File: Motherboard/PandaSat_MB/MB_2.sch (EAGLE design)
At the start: 122 parts, among them J1 503182-1852, J10 1445055-5, J2 10118194-0001LF, J3 DCJ0303, J4 1445055-5, J5 1445055-5, J6 1445055-5, J7 BK-18650, J8 1445055-5, J9 1445055-5, Q10 IRLML5103, Q11 IRLML5103, Q13 IRLML2803, Q14 IRLML2803, Q15 IRLML2803, Q16 IRLML5103, Q17 2N5088, Q2 32.768, U1 MAX706R, U11 DRV8848, U12 DRV8848, U13 DRV8848, U2 LTC4121-4.2, U3 LSM9DS1, U4 PE014006, U5 MAX4372TEUK+T, U6 RFM23BP, U7 TPS54226PWPRPWP14_2P31X2P46-L, U8 ATSAMD51, U9 OKL-T3-W12, X1 BU-SMA-V

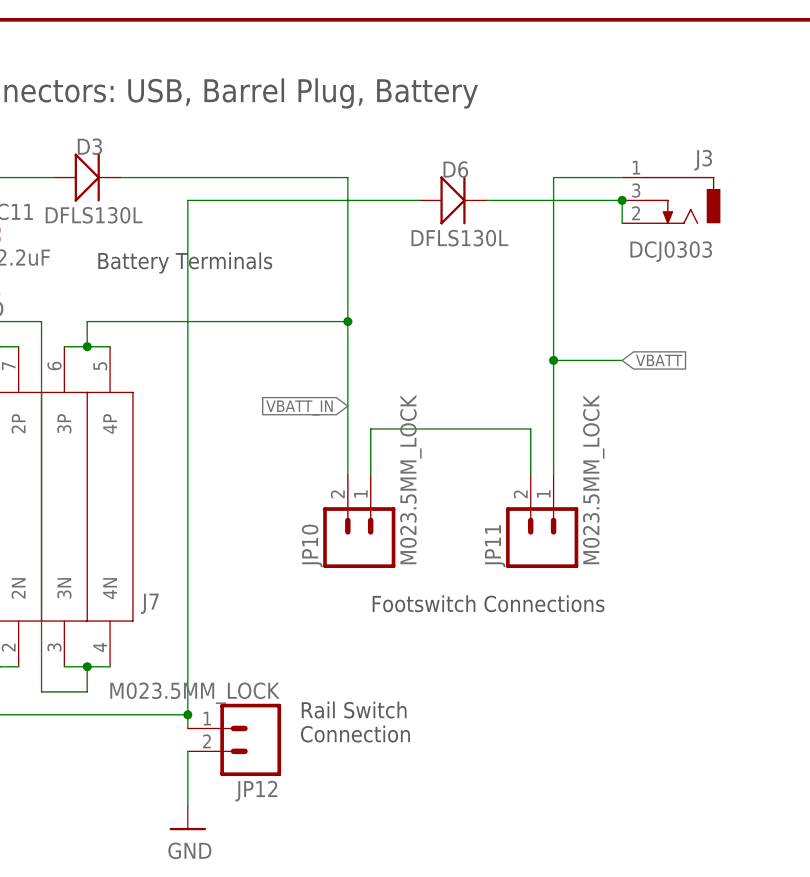
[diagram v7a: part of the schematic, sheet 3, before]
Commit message: Changed diode on power jack
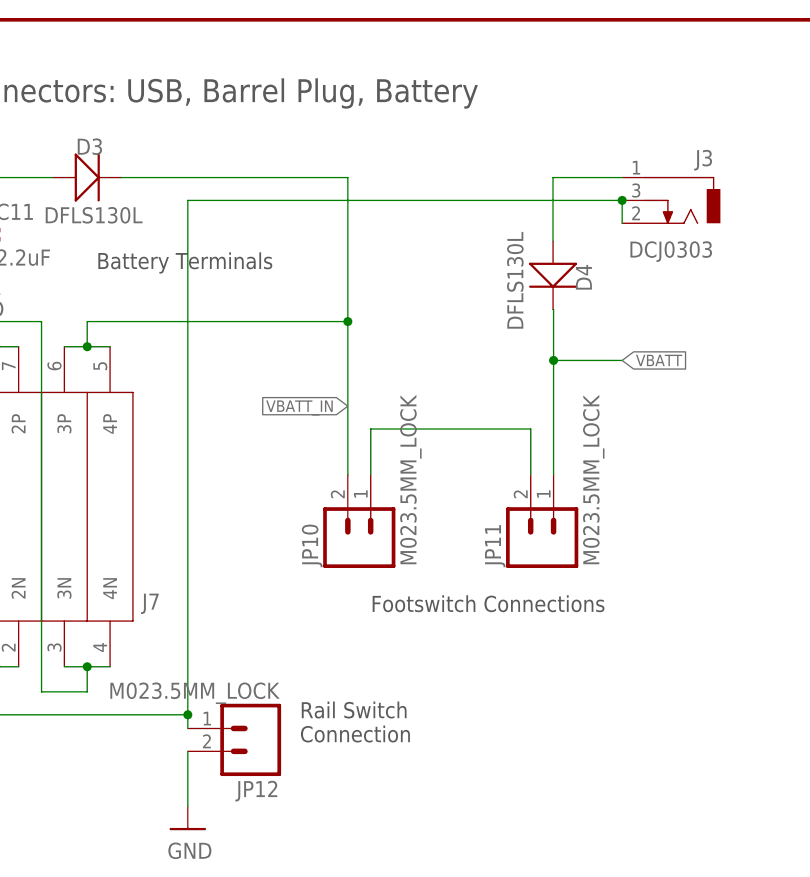
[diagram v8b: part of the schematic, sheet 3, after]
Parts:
- removed D6: DFLS130L, BrownSpaceEngineering:DFLS130L
- added D4: DFLS130L, BrownSpaceEngineering:DFLS130L
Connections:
- net N$30: now also J7.1N, J7.2N, JP12.1; no longer D6.C
- net N$40: now also D4.A, J3.1; no longer D6.A, J7.1N, J7.2N, JP12.1
- net VBATT: now also D4.C; no longer J3.1
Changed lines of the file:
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@@
 <setting verticaltext="up"/>
 </settings>
-<grid distance="2" unitdist="mm" unit="mm" style="lines" multiple="1" display="yes" altdistance="0.01" altunitdist="inch" altunit="inch"/>
+<grid distance="0.01" unitdist="inch" unit="inch" style="lines" multiple="1" display="yes" altdistance="0.01" altunitdist="inch" altunit="inch"/>
 <layers>
 <layer number="1" name="Top" color="35" fill="1" visible="no" active="no"/>
@@
 <part name="D3" library="BrownSpaceEngineering" deviceset="DFLS130L" device="" value="DFLS130L"/>
 <part name="J7" library="pandasat" deviceset="BK-18650" device=""/>
-<part name="D6" library="BrownSpaceEngineering" deviceset="DFLS130L" device="" value="DFLS130L"/>
 <part name="SUPPLY7" library="SparkFun-Aesthetics" deviceset="5V" device=""/>
 <part name="GND32" library="SparkFun-Aesthetics" deviceset="GND" device=""/>
@@
 <part name="GND39" library="supply1" library_urn="urn:adsk.eagle:library:371" deviceset="GND" device=""/>
 <part name="GND40" library="supply1" library_urn="urn:adsk.eagle:library:371" deviceset="GND" device=""/>
+<part name="D4" library="BrownSpaceEngineering" deviceset="DFLS130L" device="" value="DFLS130L"/>
 </parts>
 <sheets>
@@
 <attribute name="VALUE" x="136.652" y="143.51" size="1.778" layer="96" rot="R180"/>
 </instance>
-<instance part="D6" gate="G$1" x="193.04" y="165.354" smashed="yes">
-<attribute name="NAME" x="193.04" y="167.894" size="1.778" layer="95"/>
-<attribute name="VALUE" x="189.484" y="160.274" size="1.778" layer="96"/>
-</instance>
 <instance part="J5" gate="G$1" x="89.916" y="42.926" smashed="yes" rot="R180">
 <attribute name="NAME" x="92.456" y="46.736" size="1.778" layer="95" rot="R180"/>
@@
 <attribute name="VALUE" x="23.876" y="5.08" size="1.778" layer="96"/>
 <attribute name="NAME" x="24.384" y="21.082" size="1.778" layer="95"/>
+</instance>
+<instance part="D4" gate="G$1" x="205.426" y="158.31" smashed="yes" rot="R270">
+<attribute name="NAME" x="207.966" y="158.31" size="1.778" layer="95" rot="R270"/>
+<attribute name="VALUE" x="200.346" y="161.866" size="1.778" layer="96" rot="R270"/>
 </instance>
 </instances>
@@
 <wire x1="205.486" y1="147.574" x2="213.106" y2="147.574" width="0.1524" layer="91"/>
 <label x="213.106" y="147.574" size="1.27" layer="95" xref="yes"/>
-<pinref part="J3" gate="G$1" pin="1"/>
-<wire x1="213.106" y1="167.894" x2="205.486" y2="167.894" width="0.1524" layer="91"/>
-<wire x1="205.486" y1="167.894" x2="205.486" y2="147.574" width="0.1524" layer="91"/>
+<pinref part="D4" gate="G$1" pin="C"/>
+<wire x1="205.426" y1="153.23" x2="205.486" y2="153.23" width="0.1524" layer="91"/>
+<wire x1="205.486" y1="153.23" x2="205.486" y2="147.574" width="0.1524" layer="91"/>
 <junction x="205.486" y="147.574"/>
 </segment>
@@
 <pinref part="J3" gate="G$1" pin="2"/>
 <wire x1="213.106" y1="162.814" x2="213.106" y2="165.354" width="0.1524" layer="91"/>
-<pinref part="D6" gate="G$1" pin="C"/>
-<wire x1="198.12" y1="165.354" x2="213.106" y2="165.354" width="0.1524" layer="91"/>
+<pinref part="J7" gate="G$1" pin="1N"/>
+<pinref part="J7" gate="G$1" pin="2N"/>
+<wire x1="140.97" y1="113.538" x2="143.51" y2="113.538" width="0.1524" layer="91"/>
+<wire x1="143.51" y1="113.538" x2="146.05" y2="113.538" width="0.1524" layer="91"/>
+<wire x1="143.51" y1="113.538" x2="143.51" y2="108.204" width="0.1524" layer="91"/>
+<junction x="143.51" y="113.538"/>
+<pinref part="JP12" gate="G$1" pin="1"/>
+<wire x1="164.846" y1="106.68" x2="164.846" y2="108.204" width="0.1524" layer="91"/>
+<wire x1="143.51" y1="108.204" x2="164.846" y2="108.204" width="0.1524" layer="91"/>
+<wire x1="213.106" y1="165.354" x2="164.846" y2="165.354" width="0.1524" layer="91"/>
+<wire x1="164.846" y1="165.354" x2="164.846" y2="108.204" width="0.1524" layer="91"/>
 <junction x="213.106" y="165.354"/>
+<junction x="164.846" y="108.204"/>
 </segment>
 </net>
@@
 <wire x1="72.39" y1="32.258" x2="72.39" y2="33.782" width="0.1524" layer="91" style="longdash"/>
 <wire x1="72.39" y1="33.782" x2="0" y2="33.782" width="0.1524" layer="91" style="longdash"/>
-</segment>
-</net>
-<net name="N$40" class="0">
-<segment>
-<pinref part="J7" gate="G$1" pin="1N"/>
-<pinref part="J7" gate="G$1" pin="2N"/>
-<wire x1="140.97" y1="113.538" x2="143.51" y2="113.538" width="0.1524" layer="91"/>
-<wire x1="143.51" y1="113.538" x2="146.05" y2="113.538" width="0.1524" layer="91"/>
-<wire x1="143.51" y1="113.538" x2="143.51" y2="108.204" width="0.1524" layer="91"/>
-<junction x="143.51" y="113.538"/>
-<pinref part="JP12" gate="G$1" pin="1"/>
-<wire x1="164.846" y1="106.68" x2="164.846" y2="108.204" width="0.1524" layer="91"/>
-<pinref part="D6" gate="G$1" pin="A"/>
-<wire x1="164.846" y1="108.204" x2="164.846" y2="165.354" width="0.1524" layer="91"/>
-<wire x1="190.5" y1="165.354" x2="164.846" y2="165.354" width="0.1524" layer="91"/>
-<wire x1="143.51" y1="108.204" x2="164.846" y2="108.204" width="0.1524" layer="91"/>
-<junction x="164.846" y="108.204"/>
 </segment>
 </net>
@@
 </segment>
 </net>
+<net name="N$40" class="0">
+<segment>
+<pinref part="J3" gate="G$1" pin="1"/>
+<wire x1="213.106" y1="167.894" x2="205.426" y2="167.894" width="0.1524" layer="91"/>
+<pinref part="D4" gate="G$1" pin="A"/>
+<wire x1="205.426" y1="160.85" x2="205.426" y2="167.894" width="0.1524" layer="91"/>
+</segment>
+</net>
